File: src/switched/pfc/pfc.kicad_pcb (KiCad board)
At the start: 2 copper layers, 100 x 90.8 mm, 70 parts, among them J1 AC-input, J2 Conn_01x02, J3 Conn_01x02, Q1 STB26NM60N, U1 AP3917B, U2 bd7692fj

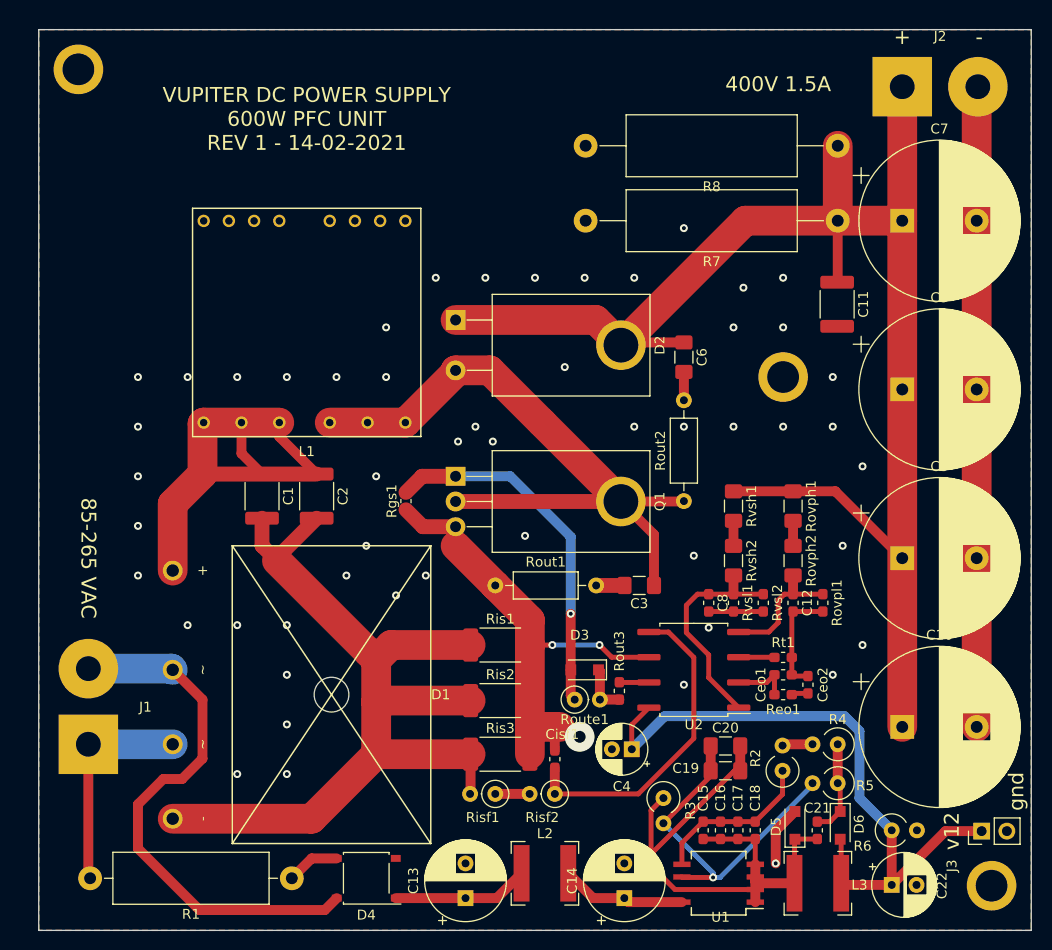
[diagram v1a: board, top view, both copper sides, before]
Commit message: footprint fix for AC input
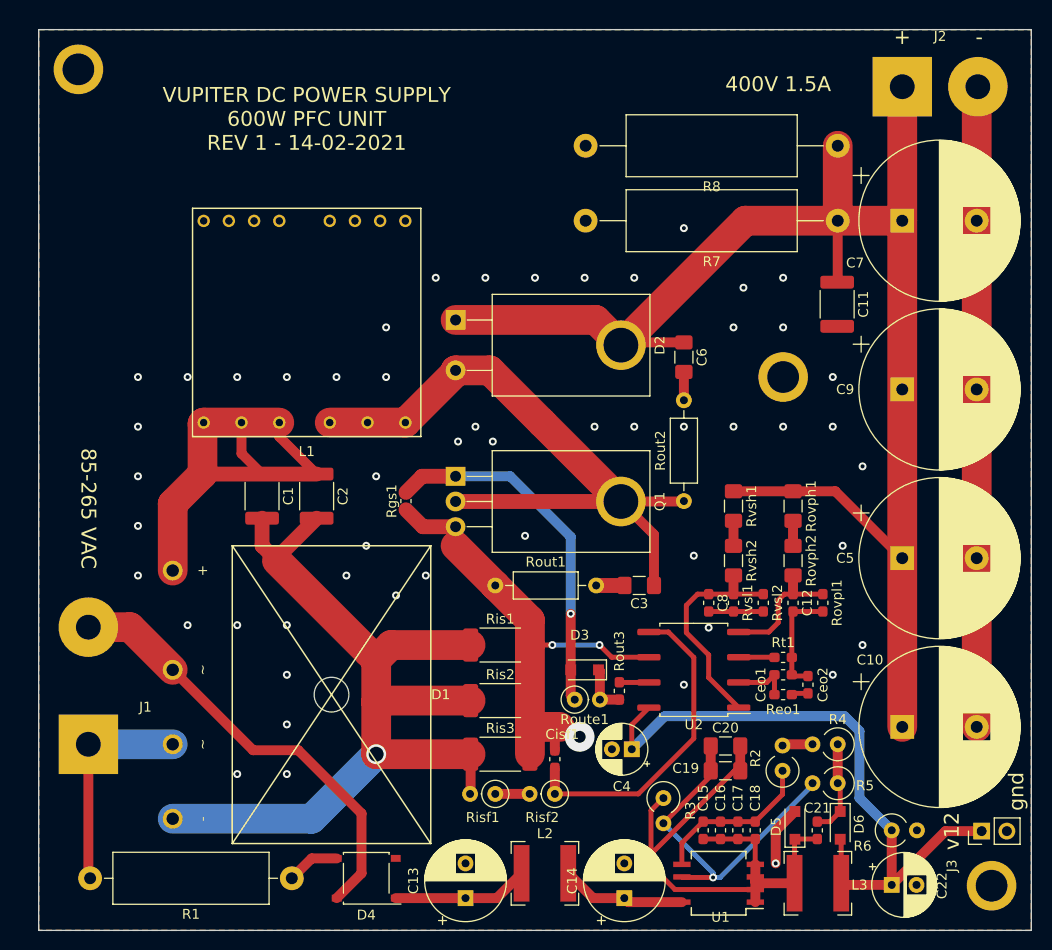
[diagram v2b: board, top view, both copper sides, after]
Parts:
- J1: footprint KiCad/kicad-footprints/Connector_Wire.pretty:SolderWirePad_1x02_P7.62mm_Drill2.5mm -> custom:spacedConnector
- Q1: value STB26NM60N -> AOT190A60CL‎
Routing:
- net v120n: track 54.7 -> 44.9 mm
- net Net-(C1-Pad2): vias 0 -> 1
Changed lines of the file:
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@@
     (thickness 1.6)
     (drawings 11)
-    (tracks 274)
+    (tracks 272)
     (zones 0)
     (modules 70)
@@
   )
   (setup
-    (last_trace_width 0.25)
+    (last_trace_width 1)
     (user_trace_width 0.5)
     (user_trace_width 1)
@@
     (via_min_size 0.4)
     (via_min_drill 0.3)
+    (user_via 2 1.5)
     (uvia_size 0.3)
     (uvia_drill 0.1)
@@
     (add_net vpfc)
   )
+  (module custom:spacedConnector (layer F.Cu)
+    (at 105 122 90)
+    (descr "Wire solder connection")
+    (tags connector)
+    (attr virtual)
+    (fp_text reference J1 (at 3.75 5.75) (layer F.SilkS)
+      (effects (font (size 1 1) (thickness 0.15)))
+    )
+    (fp_text value AC-input (at 3.81 4.445 90) (layer F.Fab)
+      (effects (font (size 1 1) (thickness 0.15)))
+    )
+    (fp_text user %R (at 3.81 0 90) (layer F.Fab)
+      (effects (font (size 1 1) (thickness 0.15)))
+    )
+    (fp_line (start -3.5 -3.5) (end 14.9 -3.5) (layer F.CrtYd) (width 0.05))
+    (fp_line (start -3.5 -3.5) (end -3.5 3.5) (layer F.CrtYd) (width 0.05))
+    (fp_line (start 14.9 3.5) (end 14.9 -3.5) (layer F.CrtYd) (width 0.05))
+    (fp_line (start 14.9 3.5) (end -3.5 3.5) (layer F.CrtYd) (width 0.05))
+    (pad 1 thru_hole rect (at 0 0 90) (size 5.99948 5.99948) (drill 2.49936) (layers *.Cu *.Mask)
+      (net 2 v120p))
+    (pad 2 thru_hole circle (at 11.8 0 90) (size 5.99948 5.99948) (drill 2.49936) (layers *.Cu *.Mask)
+      (net 1 v120n))
+  )
   (module custom:CPVPQ20161S14PZ (layer F.Cu)
     (at 127 79.5)
@@
       (effects (font (size 1 1) (thickness 0.15)))
     )
-    (fp_text value STB26NM60N (at 2.54 2 90) (layer F.Fab)
+    (fp_text value AOT190A60CL‎ (at 2.54 2 90) (layer F.Fab)
       (effects (font (size 1 1) (thickness 0.15)))
     )
@@
     (descr "CP, Radial series, Radial, pin pitch=7.50mm, , diameter=16mm, Electrolytic Capacitor")
     (tags "CP Radial series Radial pin pitch 7.50mm  diameter 16mm Electrolytic Capacitor")
-    (fp_text reference C10 (at 3.75 -9.25) (layer F.SilkS)
+    (fp_text reference C10 (at -3.25 -6.75) (layer F.SilkS)
       (effects (font (size 1 1) (thickness 0.15)))
     )
@@
     (descr "CP, Radial series, Radial, pin pitch=7.50mm, , diameter=16mm, Electrolytic Capacitor")
     (tags "CP Radial series Radial pin pitch 7.50mm  diameter 16mm Electrolytic Capacitor")
-    (fp_text reference C9 (at 3.75 -9.25) (layer F.SilkS)
+    (fp_text reference C9 (at -5.75 0) (layer F.SilkS)
       (effects (font (size 1 1) (thickness 0.15)))
     )
@@
     (descr "CP, Radial series, Radial, pin pitch=7.50mm, , diameter=16mm, Electrolytic Capacitor")
     (tags "CP Radial series Radial pin pitch 7.50mm  diameter 16mm Electrolytic Capacitor")
-    (fp_text reference C7 (at 3.75 -9.25) (layer F.SilkS)
+    (fp_text reference C7 (at -4.75 4.25) (layer F.SilkS)
       (effects (font (size 1 1) (thickness 0.15)))
     )
@@
     (descr "CP, Radial series, Radial, pin pitch=7.50mm, , diameter=16mm, Electrolytic Capacitor")
     (tags "CP Radial series Radial pin pitch 7.50mm  diameter 16mm Electrolytic Capacitor")
-    (fp_text reference C5 (at 3.75 -9.25) (layer F.SilkS)
+    (fp_text reference C5 (at -5.75 0) (layer F.SilkS)
       (effects (font (size 1 1) (thickness 0.15)))
     )
@@
     )
   )
-  (module KiCad/kicad-footprints/Connector_Wire.pretty:SolderWirePad_1x02_P7.62mm_Drill2.5mm (layer F.Cu)
-    (at 105 122 90)
-    (descr "Wire solder connection")
-    (tags connector)
-    (attr virtual)
-    (fp_text reference J1 (at 3.75 5.75 180) (layer F.SilkS)
-      (effects (font (size 1 1) (thickness 0.15)))
-    )
-    (fp_text value AC-input (at 3.81 4.445 90) (layer F.Fab)
-      (effects (font (size 1 1) (thickness 0.15)))
-    )
-    (fp_line (start -3.5 -3.5) (end 11.12 -3.5) (layer F.CrtYd) (width 0.05))
-    (fp_line (start -3.5 -3.5) (end -3.5 3.5) (layer F.CrtYd) (width 0.05))
-    (fp_line (start 11.12 3.5) (end 11.12 -3.5) (layer F.CrtYd) (width 0.05))
-    (fp_line (start 11.12 3.5) (end -3.5 3.5) (layer F.CrtYd) (width 0.05))
-    (fp_text user %R (at 3.81 0 90) (layer F.Fab)
-      (effects (font (size 1 1) (thickness 0.15)))
-    )
-    (pad 2 thru_hole circle (at 7.62 0 90) (size 5.99948 5.99948) (drill 2.49936) (layers *.Cu *.Mask)
-      (net 1 v120n))
-    (pad 1 thru_hole rect (at 0 0 90) (size 5.99948 5.99948) (drill 2.49936) (layers *.Cu *.Mask)
-      (net 2 v120p))
-  )
   (gr_text "VUPITER DC POWER SUPPLY\n600W PFC UNIT\nREV 1 - 14-02-2021" (at 127 59) (layer F.SilkS)
     (effects (font (size 1.5 1.5) (thickness 0.3)))
@@
     (effects (font (size 1.5 1.5) (thickness 0.3)))
   )
-  (gr_text "85-265 VAC" (at 105 103.25 270) (layer F.SilkS)
+  (gr_text "85-265 VAC" (at 105 98.25 270) (layer F.SilkS)
     (effects (font (size 1.5 1.5) (thickness 0.3)))
   )
@@
   (gr_line (start 200 50) (end 200 140.75) (layer Edge.Cuts) (width 0.05))
   (gr_line (start 100 50) (end 200 50) (layer Edge.Cuts) (width 0.05))
-  (segment (start 113.38 114.38) (end 113.5 114.5) (width 3) (layer B.Cu) (net 1))
-  (segment (start 105 114.38) (end 113.38 114.38) (width 3) (layer B.Cu) (net 1))
-  (segment (start 109.99999 128.050249) (end 112.550239 125.5) (width 1) (layer F.Cu) (net 1))
-  (segment (start 109.99999 132.49999) (end 109.99999 128.050249) (width 1) (layer F.Cu) (net 1))
-  (segment (start 116.500001 117.500001) (end 113.5 114.5) (width 1) (layer F.Cu) (net 1))
-  (segment (start 116.500001 123.440001) (end 116.500001 117.500001) (width 1) (layer F.Cu) (net 1))
-  (segment (start 114.440002 125.5) (end 116.500001 123.440001) (width 1) (layer F.Cu) (net 1))
-  (segment (start 112.550239 125.5) (end 114.440002 125.5) (width 1) (layer F.Cu) (net 1))
-  (segment (start 128.824999 138.700001) (end 130.025 137.5) (width 1) (layer F.Cu) (net 1))
-  (segment (start 116.200001 138.700001) (end 128.824999 138.700001) (width 1) (layer F.Cu) (net 1))
-  (segment (start 109.99999 132.49999) (end 116.200001 138.700001) (width 1) (layer F.Cu) (net 1))
+  (segment (start 109.2 110.2) (end 113.5 114.5) (width 3) (layer F.Cu) (net 1))
+  (segment (start 105 110.2) (end 109.2 110.2) (width 3) (layer F.Cu) (net 1))
+  (segment (start 132.525001 134.999999) (end 130.025 137.5) (width 1) (layer F.Cu) (net 1))
+  (segment (start 126.152001 122.599999) (end 132.525001 128.972999) (width 1) (layer F.Cu) (net 1))
+  (segment (start 121.599999 122.599999) (end 126.152001 122.599999) (width 1) (layer F.Cu) (net 1))
+  (segment (start 132.525001 128.972999) (end 132.525001 134.999999) (width 1) (layer F.Cu) (net 1))
+  (segment (start 113.5 114.5) (end 121.599999 122.599999) (width 1) (layer F.Cu) (net 1))
   (segment (start 105 122) (end 113.5 122) (width 3) (layer B.Cu) (net 2))
   (segment (start 105 135.32) (end 105.18 135.5) (width 1) (layer F.Cu) (net 2))
@@
   (segment (start 143.5125 126.9475) (end 143.46 127) (width 1) (layer F.Cu) (net 3))
   (segment (start 143.5125 123) (end 143.5125 126.9475) (width 1) (layer F.Cu) (net 3))
-  (segment (start 127.5 129.5) (end 113.5 129.5) (width 3) (layer F.Cu) (net 3))
-  (segment (start 134 123) (end 127.5 129.5) (width 3) (layer F.Cu) (net 3))
   (segment (start 143.5125 123) (end 134 123) (width 3) (layer F.Cu) (net 3))
   (segment (start 134 113.5) (end 133.200001 112.700001) (width 3) (layer F.Cu) (net 3))
@@
   (segment (start 134 117.75) (end 134 113.5) (width 3) (layer F.Cu) (net 3))
   (segment (start 134 123) (end 134 117.75) (width 3) (layer F.Cu) (net 3))
+  (segment (start 134 123) (end 134 123) (width 3) (layer F.Cu) (net 3))
+  (via (at 134 123) (size 2) (drill 1.5) (layers F.Cu B.Cu) (net 3))
+  (segment (start 127.5 129.5) (end 134 123) (width 3) (layer B.Cu) (net 3))
+  (segment (start 113.5 129.5) (end 127.5 129.5) (width 3) (layer B.Cu) (net 3))
   (segment (start 113.5 97.77879) (end 116.50379 94.775) (width 3) (layer F.Cu) (net 4))
   (segment (start 113.5 104.5) (end 113.5 97.77879) (width 3) (layer F.Cu) (net 4))
@@
   (via (at 134 95) (size 0.8) (drill 0.4) (layers F.Cu B.Cu) (net 7))
   (via (at 144 90) (size 0.8) (drill 0.4) (layers F.Cu B.Cu) (net 7))
-  (via (at 153 84) (size 0.8) (drill 0.4) (layers F.Cu B.Cu) (net 7))
+  (via (at 156 90) (size 0.8) (drill 0.4) (layers F.Cu B.Cu) (net 7))
   (via (at 183 94) (size 0.8) (drill 0.4) (layers F.Cu B.Cu) (net 7))
   (via (at 181 102) (size 0.8) (drill 0.4) (layers F.Cu B.Cu) (net 7))

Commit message: fixing the pfc footprints and relating them to their lcsc counterparts
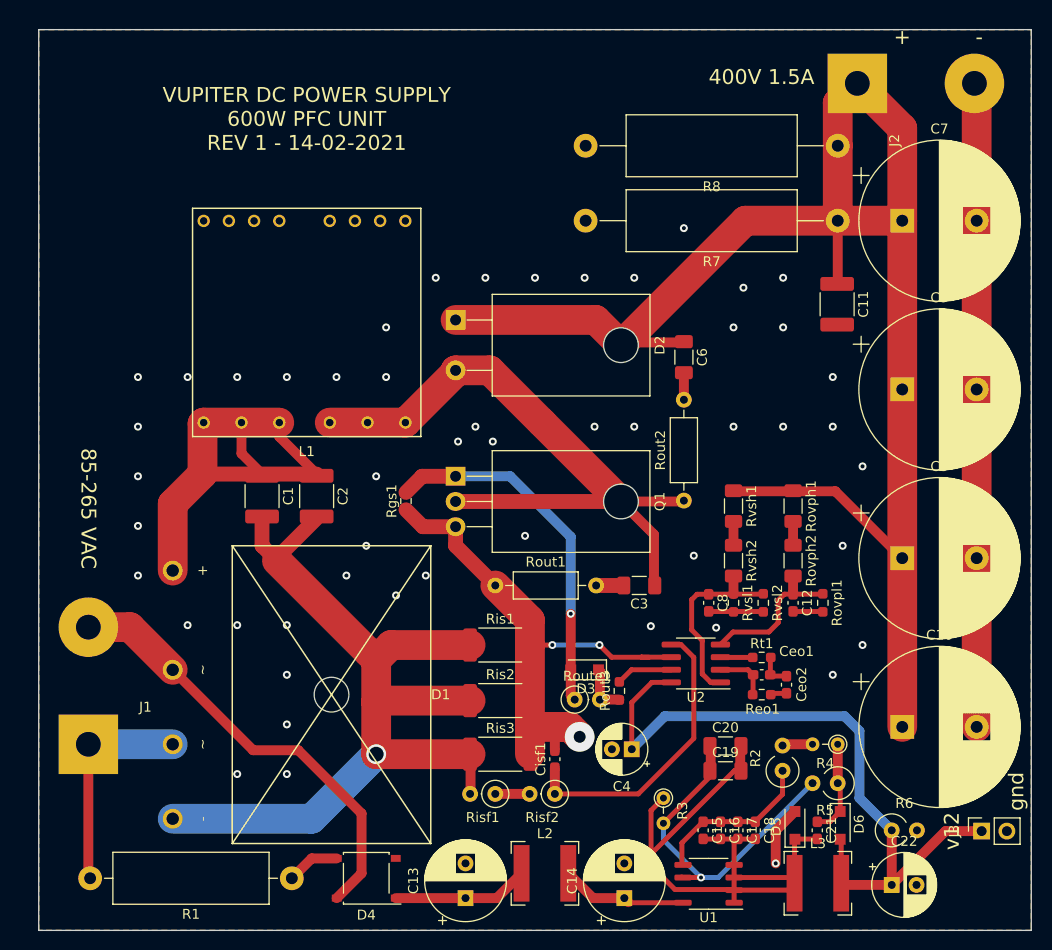
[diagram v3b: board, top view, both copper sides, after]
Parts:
- removed REF** (x3): MountingHole_3.2mm_M3, KiCad/kicad-footprints/MountingHole.pretty:MountingHole_3.2mm_M3
- C1, C11, C2: footprint KiCad/kicad-footprints/Capacitor_SMD.pretty:C_1812_4532Metric_Pad1.30x3.40mm_HandSolder -> Capacitor_SMD:C_1812_4532Metric
- C10, C5, C7, C9: footprint KiCad/kicad-footprints/Capacitor_THT.pretty:CP_Radial_D16.0mm_P7.50mm -> Capacitor_THT:CP_Radial_D16.0mm_P7.50mm
- C12, C15, C16, C17, C18, C21, C8, Ceo1, Ceo2, Cisf1: footprint KiCad/kicad-footprints/Capacitor_SMD.pretty:C_0603_1608Metric_Pad1.05x0.95mm_HandSolder -> Capacitor_SMD:C_0603_1608Metric_Pad1.08x0.95mm_HandSolder
- C13, C14: footprint KiCad/kicad-footprints/Capacitor_THT.pretty:CP_Radial_D8.0mm_P3.50mm -> Capacitor_THT:CP_Radial_D8.0mm_P3.50mm
- C19, C20, C3, C6: footprint KiCad/kicad-footprints/Capacitor_SMD.pretty:C_1206_3216Metric_Pad1.42x1.75mm_HandSolder -> Capacitor_SMD:C_1206_3216Metric_Pad1.33x1.80mm_HandSolder
- C22: footprint KiCad/kicad-footprints/Capacitor_THT.pretty:CP_Radial_D6.3mm_P2.50mm -> Capacitor_THT:CP_Radial_D6.3mm_P2.50mm
- C4: footprint KiCad/kicad-footprints/Capacitor_THT.pretty:CP_Radial_D5.0mm_P2.00mm -> Capacitor_THT:CP_Radial_D5.0mm_P2.00mm
- D2: footprint KiCad/kicad-footprints/Package_TO_SOT_THT.pretty:TO-220-2_Horizontal_TabDown -> Package_TO_SOT_THT:TO-220-2_Horizontal_TabDown
- D3, D5, D6: footprint KiCad/kicad-footprints/Diode_SMD.pretty:D_SOD-123F -> Diode_SMD:D_SOD-123F
- D4: footprint KiCad/kicad-footprints/Diode_SMD.pretty:Diode_Bridge_Diotec_ABS -> Diode_SMD:Diode_Bridge_Diotec_ABS
- J2: footprint KiCad/kicad-footprints/Connector_Wire.pretty:SolderWirePad_1x02_P7.62mm_Drill2.5mm -> custom:spacedConnector
- J3: footprint KiCad/kicad-footprints/Connector_PinHeader_2.54mm.pretty:PinHeader_1x02_P2.54mm_Vertical -> Connector_PinSocket_2.54mm:PinSocket_1x02_P2.54mm_Vertical
- L2, L3: footprint KiCad/kicad-footprints/Inductor_SMD.pretty:L_Bourns-SRN6028 -> Inductor_SMD:L_Bourns-SRN6028
- Q1: footprint KiCad/kicad-footprints/Package_TO_SOT_THT.pretty:TO-220-3_Horizontal_TabDown -> Package_TO_SOT_THT:TO-220-3_Horizontal_TabDown
- R1: footprint KiCad/kicad-footprints/Resistor_THT.pretty:R_Axial_DIN0516_L15.5mm_D5.0mm_P20.32mm_Horizontal -> Resistor_THT:R_Axial_DIN0516_L15.5mm_D5.0mm_P20.32mm_Horizontal
- R2, R5, R6: footprint KiCad/kicad-footprints/Resistor_THT.pretty:R_Axial_DIN0309_L9.0mm_D3.2mm_P2.54mm_Vertical -> Resistor_THT:R_Axial_DIN0309_L9.0mm_D3.2mm_P2.54mm_Vertical
- R3, R4: value 5.62k -> 5.6k; footprint KiCad/kicad-footprints/Resistor_THT.pretty:R_Axial_DIN0309_L9.0mm_D3.2mm_P2.54mm_Vertical -> Resistor_THT:R_Axial_DIN0204_L3.6mm_D1.6mm_P2.54mm_Vertical
- R7, R8: footprint KiCad/kicad-footprints/Resistor_THT.pretty:R_Axial_DIN0617_L17.0mm_D6.0mm_P25.40mm_Horizontal -> Resistor_THT:R_Axial_DIN0617_L17.0mm_D6.0mm_P25.40mm_Horizontal
- Reo1, Rgs1, Rout3, Rovpl1, Rt1, Rvsl1, Rvsl2: footprint KiCad/kicad-footprints/Resistor_SMD.pretty:R_0603_1608Metric_Pad1.05x0.95mm_HandSolder -> Resistor_SMD:R_0603_1608Metric_Pad0.98x0.95mm_HandSolder
- Ris1, Ris2, Ris3: footprint KiCad/kicad-footprints/Capacitor_SMD.pretty:C_2512_6332Metric_Pad1.52x3.35mm_HandSolder -> Resistor_SMD:R_2512_6332Metric_Pad1.40x3.35mm_HandSolder
- Risf1, Risf2, Route1: value 50 -> 51; footprint KiCad/kicad-footprints/Resistor_THT.pretty:R_Axial_DIN0207_L6.3mm_D2.5mm_P2.54mm_Vertical -> Resistor_THT:R_Axial_DIN0207_L6.3mm_D2.5mm_P2.54mm_Vertical
- Rout1, Rout2: value 50 -> 51; footprint KiCad/kicad-footprints/Resistor_THT.pretty:R_Axial_DIN0207_L6.3mm_D2.5mm_P10.16mm_Horizontal -> Resistor_THT:R_Axial_DIN0207_L6.3mm_D2.5mm_P10.16mm_Horizontal
- Rovph1, Rovph2, Rvsh1, Rvsh2: footprint KiCad/kicad-footprints/Resistor_SMD.pretty:R_1206_3216Metric_Pad1.42x1.75mm_HandSolder -> Resistor_SMD:R_1206_3216Metric_Pad1.30x1.75mm_HandSolder
- U1: footprint custom:SO-7_5.3x6.2mm_P1.27mm -> custom:SO-7_3.9x4.9mm_P1.27mm
- U2: footprint KiCad/kicad-footprints/Package_SO.pretty:SOP-8_6.62x9.15mm_P2.54mm -> Package_SO:SOIC-8_3.9x4.9mm_P1.27mm
- moved J2 4.54 mm to (182.5, 55.4)
- moved Ceo1 2.16 mm to (172.8, 115.0)
- moved Ceo2 2.16 mm to (175.3, 116.0)
- moved Reo1 2.16 mm to (172.8, 117.0)
- moved Rt1 2.16 mm to (172.8, 113.2)
- moved U1 1.01 mm to (167.5, 136.1)
- moved U2 0.67 mm to (166.2, 113.9)
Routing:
- net vpfc: track 157.2 -> 166.5 mm
- net Net-(C15-Pad2): track 57.3 -> 64.1 mm
- net v12: track 68.0 -> 72.7 mm
- net vs: track 22.6 -> 19.4 mm
- net out: track 2.98 -> 5.76 mm
- net is: track 33.2 -> 30.4 mm
- net ovp: track 13.3 -> 15.6 mm
- net gnd: track 135.8 -> 138.0 mm, vias 55 -> 54
- net Net-(C19-Pad1): track 34.6 -> 33.9 mm
- net Net-(C14-Pad1): track 12.7 -> 13.4 mm

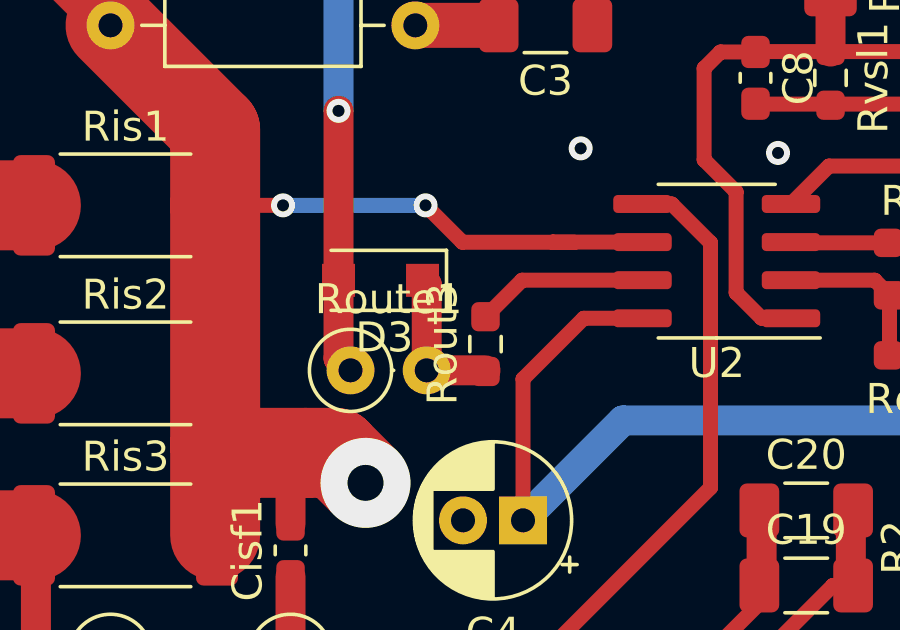
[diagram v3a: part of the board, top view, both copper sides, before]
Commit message: Faster gate drive on pfc
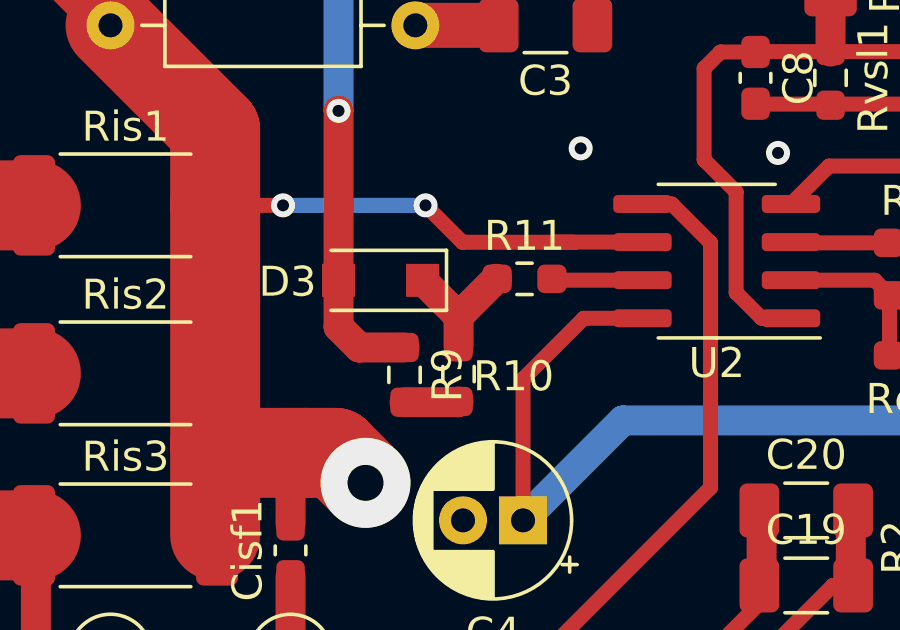
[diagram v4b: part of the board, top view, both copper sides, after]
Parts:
- removed Route1: 51, Resistor_THT:R_Axial_DIN0207_L6.3mm_D2.5mm_P2.54mm_Vertical
- added R10: 13, Resistor_SMD:R_0603_1608Metric_Pad0.98x0.95mm_HandSolder, F.Cu at (157.6, 117.6)
- added R9: 13, Resistor_SMD:R_0603_1608Metric_Pad0.98x0.95mm_HandSolder, F.Cu at (155.8, 117.7)
- R11: renamed from Rout3; value 10 -> 13
- moved R11 2.53 mm to (159.8, 114.5), turned to 0 degrees
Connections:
- net v12 renamed vcc
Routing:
- net out: track 5.76 -> 3.04 mm
- net Net-(R10-Pad1): track 0.00 -> 1.81 mm
- net Net-(D3-Pad2): track 36.4 -> 37.2 mm
- net Net-(D3-Pad1): track 5.02 -> 4.51 mm
